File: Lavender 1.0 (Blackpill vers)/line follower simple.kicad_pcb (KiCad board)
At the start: 2 copper layers, 214 x 187.9 mm, 259 parts, among them J1 XT30UPB-M, J10 Conn_01x13_Pin, J11 Conn_01x13_Pin, J12 Conn_01x13_Pin, J13 Conn_01x13_Pin, J14 Conn_01x20_MountingPin, J15 Conn_01x11_Pin, J16 Conn_01x11_Pin, J17 Conn_01x11_Pin, J18 Conn_01x11_Pin, J19 Conn_01x11_Pin, J2 Conn_01x20_MountingPin, J3 Conn_01x02_Pin, J4 Conn_01x02_Pin, J5 Conn_01x28_Pin, J6 Conn_01x20_MountingPin, J7 Conn_01x20_MountingPin, J8 Conn_01x28_Pin, J9 Conn_01x20_MountingPin, Q1 BPW40, Q2 BPW40, Q3 BPW40, Q4 BPW40, Q5 BPW40, Q6 BPW40, Q7 BPW40, Q8 BPW40, Q9 BPW40, SW2 SW_Push, SW3 SW_Push, SW5 SW_Push_DPDT, SW6 SW_Push_DPDT, U1 74HC4067, U10 QRE1113GR, U11 QRE1113GR, U12 QRE1113GR, U13 QRE1113GR, U14 QRE1113GR, U15 QRE1113GR, U16 QRE1113GR, U17 QRE1113GR, U18 QRE1113GR, U19 TCRT5000L, U2 TCRT5000L, U20 TCRT5000L, U21 QRE1113GR, U22 QRE1113GR, U23 QRE1113GR, U24 QRE1113GR, U25 QRE1113GR, U26 QRE1113GR, U27 QRE1113GR, U28 QRE1113GR, U29 QRE1113GR, U30 QRE1113GR, U31 QRE1113GR, U32 QRE1113GR, U33 QRE1113GR, U34 QRE1113GR, U35 QRE1113GR, U36 QRE1113GR, U4 TCRT5000L, U5 TCRT5000L, U6 TCRT5000L, U7 TCRT5000L, U8 TCRT5000L, U9 TCRT5000L

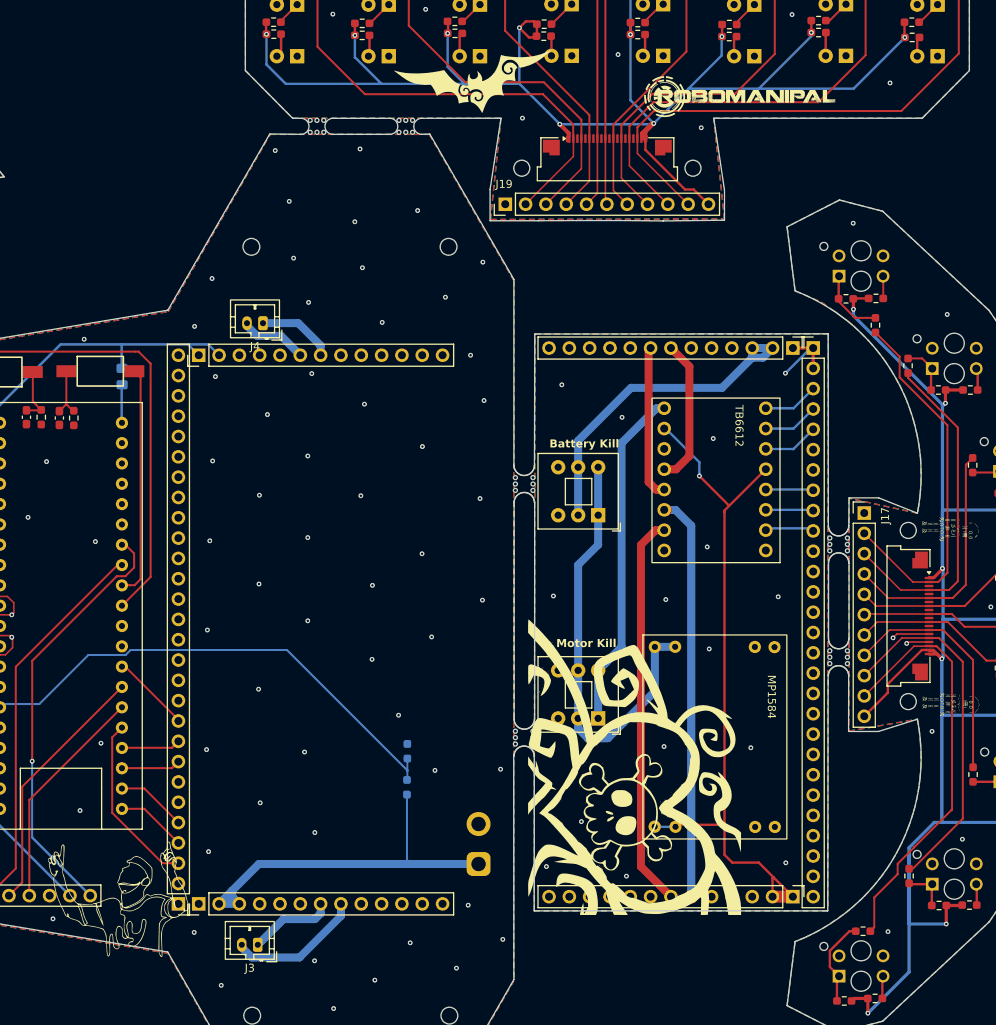
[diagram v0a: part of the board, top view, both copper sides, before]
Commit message: Fix overlapping silkscreen
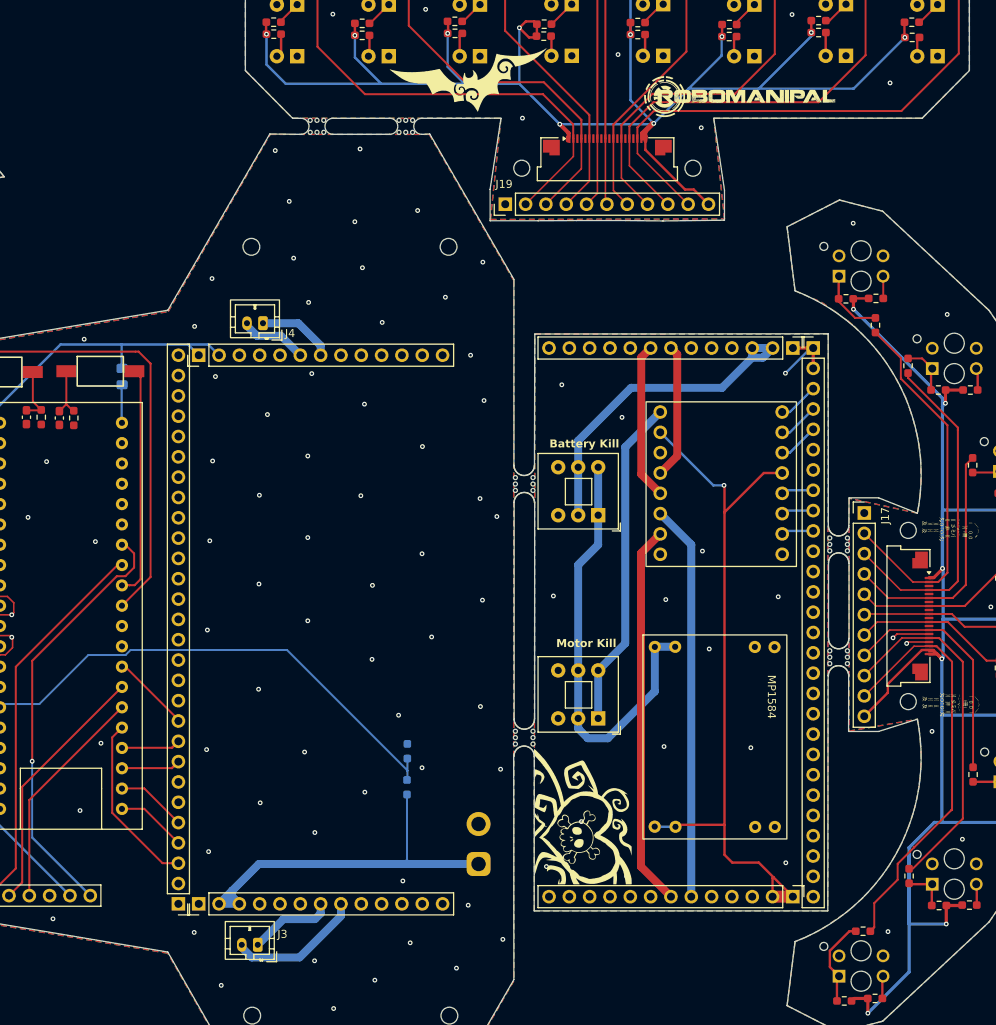
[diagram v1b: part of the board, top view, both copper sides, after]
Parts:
- G***: moved to B.Cu
- moved G*** 27.1 mm to (125.8, 136.3), turned to 180 degrees
- moved G*** 8.94 mm to (158.0, 132.1)
- moved G*** 4.05 mm to (135.4, 117.5)
- moved G*** 1.02 mm to (144.0, 88.3)
- moved G*** 1.00 mm to (204.8, 96.1)
- moved TB1 0.68 mm to (172.3, 92.6)
- moved ? 0.59 mm to (151.8, 39.5)
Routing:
- net +3.3V: track 1255.0 -> 1257.6 mm
- net AIN1_t: track 6.95 -> 5.08 mm
- net AIN2_t: track 6.74 -> 5.08 mm
- net PWMA_t: track 6.74 -> 5.08 mm
- net BIN2_t: track 5.76 -> 4.16 mm
- net BIN1_t: track 5.76 -> 4.16 mm
- net PWMB_t: track 5.94 -> 4.47 mm
- net Motor2+_t: track 49.2 -> 47.9 mm
- net Motor1+_t: track 18.1 -> 16.8 mm
- net BAT+_Driver: track 42.8 -> 41.5 mm
- net Motor2-_t: track 50.4 -> 49.5 mm
- net GND: vias 151 -> 154
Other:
- board text removed: "TB6612"
